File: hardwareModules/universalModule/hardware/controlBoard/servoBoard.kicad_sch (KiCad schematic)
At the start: 7 parts, among them J12 SHOE, J3 BOARD_IN, J4 SERVO

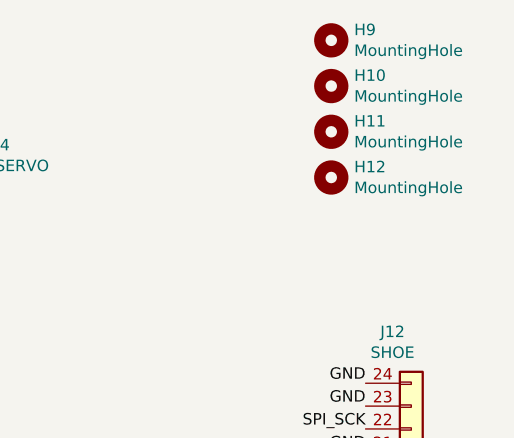
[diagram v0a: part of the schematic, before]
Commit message: um: Fix hardware bugs, prepare v0.5
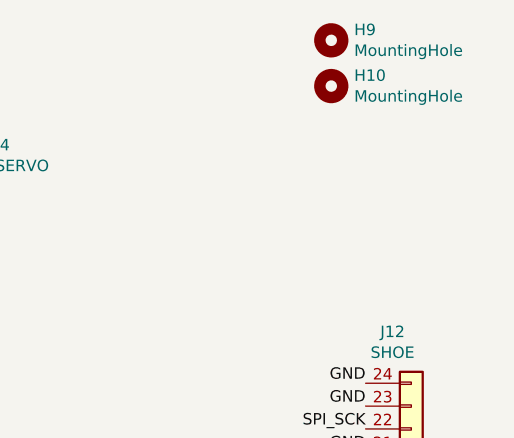
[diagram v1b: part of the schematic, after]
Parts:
- removed H11, H12: MountingHole, MountingHole:MountingHole_2.7mm, symbol Mechanical:MountingHole
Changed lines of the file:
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@@
-    )
-  )
-  (symbol (lib_id "Mechanical:MountingHole") (at 195.58 44.45 0) (unit 1)
-    (in_bom yes) (on_board yes)
-    (property "Reference" "H11" (id 0) (at 198.12 43.2816 0)
-      (effects (font (size 1.27 1.27)) (justify left))
-    )
-    (property "Value" "MountingHole" (id 1) (at 198.12 45.593 0)
-      (effects (font (size 1.27 1.27)) (justify left))
-    )
-    (property "Footprint" "MountingHole:MountingHole_2.7mm" (id 2) (at 195.58 44.45 0)
-      (effects (font (size 1.27 1.27)) hide)
-    )
-    (property "Datasheet" "~" (id 3) (at 195.58 44.45 0)
-      (effects (font (size 1.27 1.27)) hide)
-    )
-    (property "JLCPCB_IGNORE" "YES" (id 4) (at 195.58 44.45 0)
-      (effects (font (size 1.27 1.27)) hide)
-    )
-  )
-  (symbol (lib_id "Mechanical:MountingHole") (at 195.58 49.53 0) (unit 1)
-    (in_bom yes) (on_board yes)
-    (property "Reference" "H12" (id 0) (at 198.12 48.3616 0)
-      (effects (font (size 1.27 1.27)) (justify left))
-    )
-    (property "Value" "MountingHole" (id 1) (at 198.12 50.673 0)
-      (effects (font (size 1.27 1.27)) (justify left))
-    )
-    (property "Footprint" "MountingHole:MountingHole_2.7mm" (id 2) (at 195.58 49.53 0)
-      (effects (font (size 1.27 1.27)) hide)
-    )
-    (property "Datasheet" "~" (id 3) (at 195.58 49.53 0)
-      (effects (font (size 1.27 1.27)) hide)
-    )
-    (property "JLCPCB_IGNORE" "YES" (id 4) (at 195.58 49.53 0)
-      (effects (font (size 1.27 1.27)) hide)
     )
   )
